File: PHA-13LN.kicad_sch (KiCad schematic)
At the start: 14 parts, among them U2 PHA-13LN

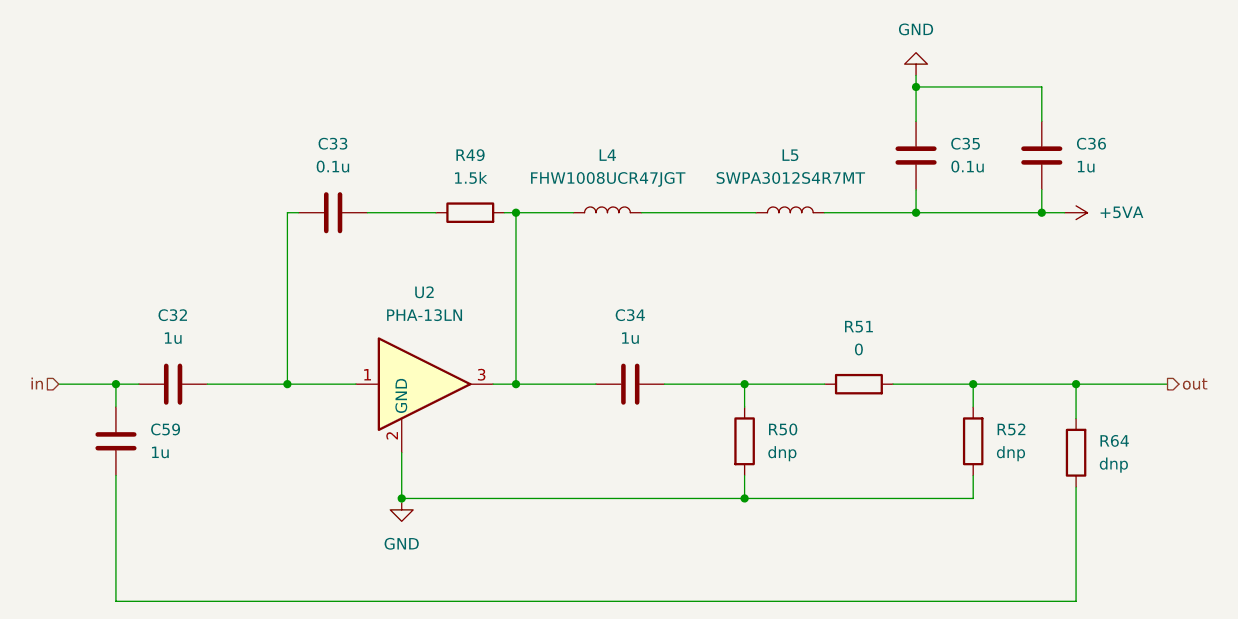
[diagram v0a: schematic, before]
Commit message: Version 1.0 submitted to JLCPCB
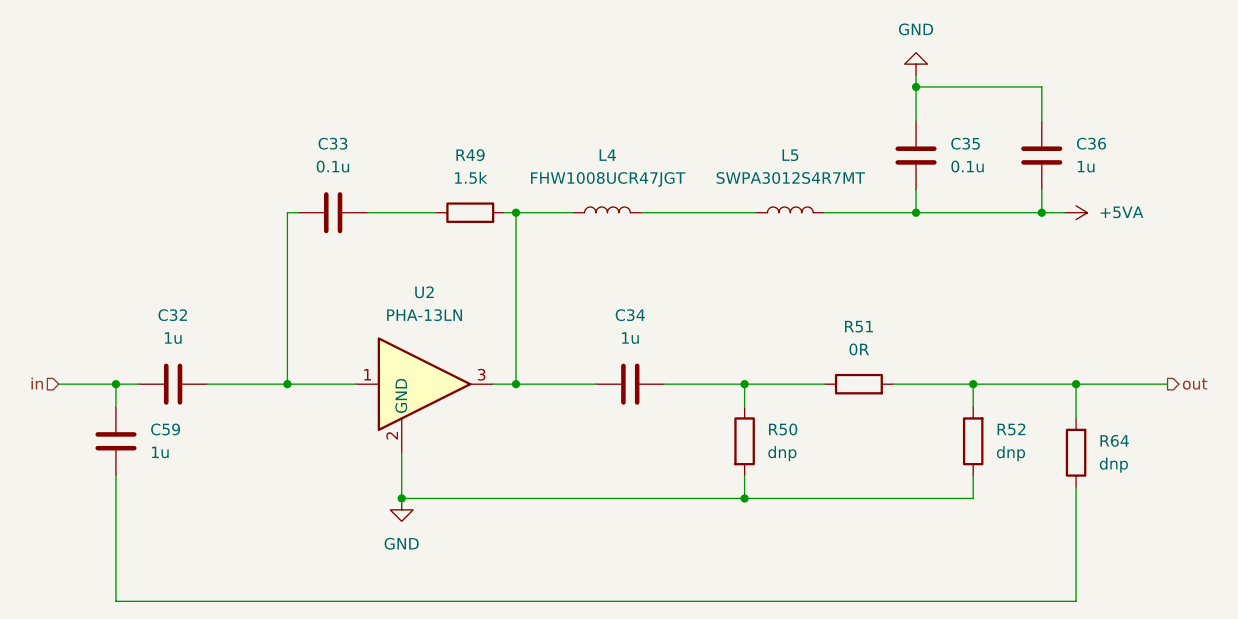
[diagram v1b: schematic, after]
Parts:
- R51: value 0 -> 0R
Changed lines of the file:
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@@
     (in_bom yes) (on_board yes) (fields_autoplaced)
     (property "Reference" "R51" (id 0) (at 166.37 74.93 90))
-    (property "Value" "0" (id 1) (at 166.37 77.47 90))
+    (property "Value" "0R" (id 1) (at 166.37 77.47 90))
     (property "Footprint" "Resistor_SMD:R_0805_2012Metric" (id 2) (at 166.37 83.058 90)
       (effects (font (size 1.27 1.27)) hide)
